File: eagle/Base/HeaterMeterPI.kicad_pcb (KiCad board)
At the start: 2 copper layers, 94.6 x 45.7 mm, 66 parts, among them IC1 OKI-78SR-5, IC2 ATmega328P, IC4 MCP1700, IC5 AD849X, J1 RPi, J2 PROBE, J4 PCC-SMP, J9 Barrel_Jack_Switch, Q1 BS170, Q2 BS170, Q3 FQU11P06TU, Q5 BS170, Y1 16MHz

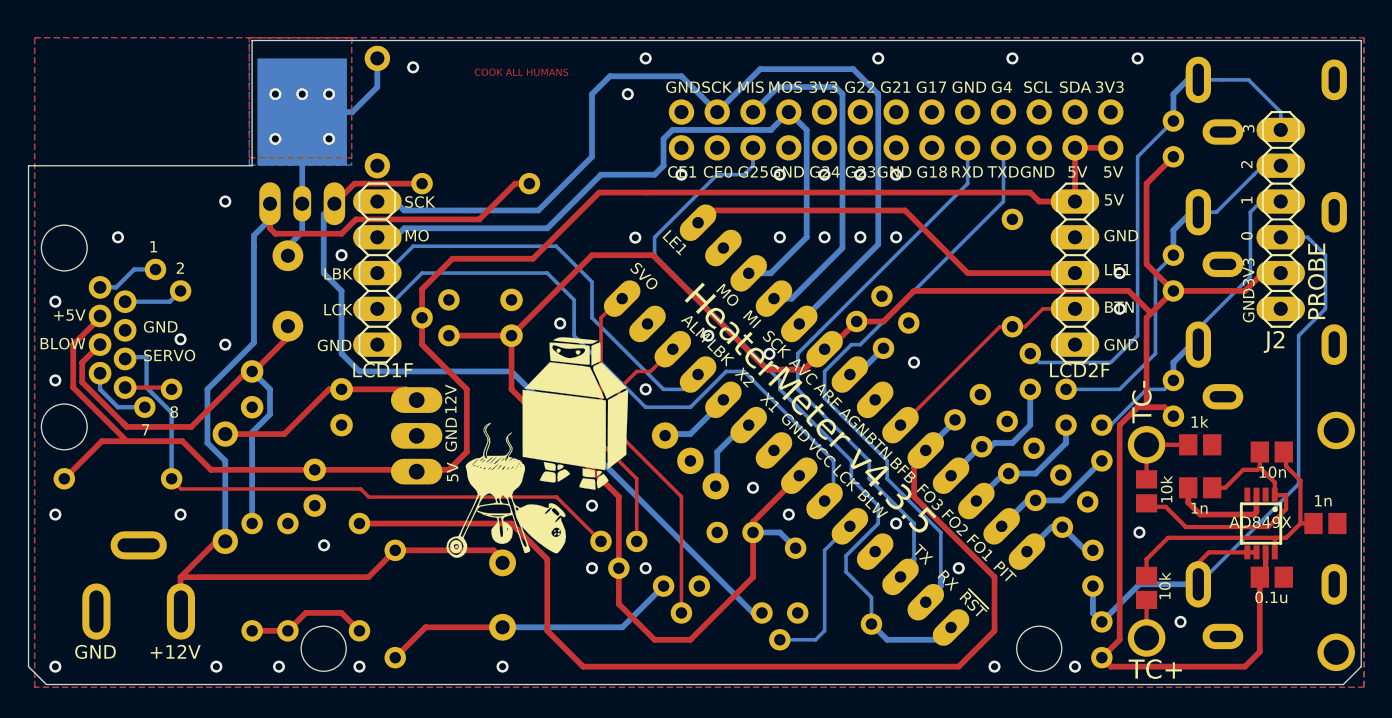
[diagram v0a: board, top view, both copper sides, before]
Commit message: [eagle] HeaterMeter Base v4.3.6
* Replace probe jacks with CUI MU1-2503A
* Thermocouple PCC-SMP-K get plated slots instead of hole
* Reduce size of RJ45 jack mounting holes for snapier fit
* Capacitors 100u/10V, 47u/25V footprint replaced with 2.0mm lead spacing
* Board slightly enlarged on top edge to fit jacks
* Thermocouple amp SMD layout revised to fit around jack
* PROBE pinheader moved to fit around jacks
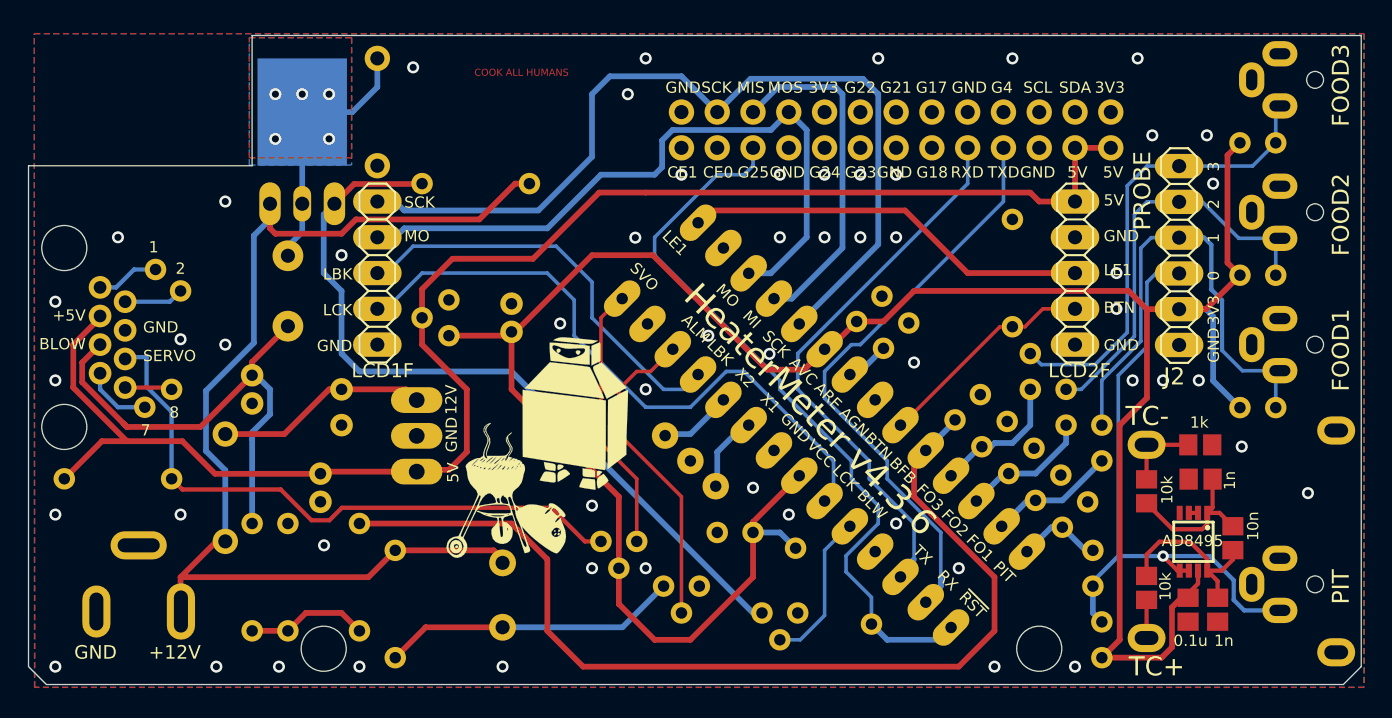
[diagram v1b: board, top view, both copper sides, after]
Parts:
- C12, C5, C6: footprint HeaterMeterPI:E2,5-5 -> HeaterMeterPI:E2-5
- IC5: value AD849X -> AD8495
- JP3, JP4, JP5, JP6: footprint HeaterMeterPI:CUI-MJ-2508 -> HeaterMeterPI:CUI-MJ1-2503A
- moved C8 9.80 mm to (185.6, 122.6), turned to 90 degrees
- moved J2 7.66 mm to (182.9, 97.4)
- moved C9 6.72 mm to (186.7, 117.5), turned to 90 degrees
- moved C13 6.38 mm to (183.5, 122.6), turned to 270 degrees
- moved R17 6.03 mm to (188.5, 108.2), turned to 180 degrees
- moved R5 6.00 mm to (188.5, 89.4), turned to 180 degrees
- moved R16 6.00 mm to (188.5, 98.8), turned to 180 degrees
- moved IC5 4.97 mm to (183.9, 117.7)
- moved JP3 3.07 mm to (192.5, 120.8)
- moved JP4 3.07 mm to (192.5, 103.7)
- moved JP5 3.07 mm to (192.5, 94.3)
- moved JP6 3.07 mm to (192.5, 84.9)
- moved C11 0.61 mm to (184.4, 113.3)
- moved C5 0.41 mm to (121.9, 113.9)
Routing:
- net Net-(J2-Pad4): track 23.4 -> 34.8 mm
- net Net-(C11-Pad1): track 20.5 -> 11.0 mm
- net Net-(C8-Pad2): track 20.7 -> 12.3 mm
- net GND: track 7.56 -> 0.65 mm, vias 51 -> 57
- net Net-(J2-Pad6): track 37.1 -> 33.0 mm
- net +3V3: track 174.3 -> 170.2 mm
- net /PIT_P: track 47.5 -> 44.4 mm, vias 0 -> 1
- net Net-(J2-Pad5): track 26.3 -> 27.6 mm
- net /SRVBST: track 43.3 -> 44.1 mm
- net /BLOWER: track 11.7 -> 11.0 mm
- net /SCK: track 64.1 -> 63.5 mm
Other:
- board size 94.6 x 45.7 mm -> 94.6 x 46.1 mm
- board text added: "HeaterMeter v4.3.6"
- board text removed: "HeaterMeter v4.3.5"
